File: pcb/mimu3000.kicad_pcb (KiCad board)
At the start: 2 copper layers, 54.9 x 25.9 mm, 14 parts, among them SW1 P_MISO, SW2 P_MOSI, U1 ATTINY13A-SSU, U2 AQY211EH

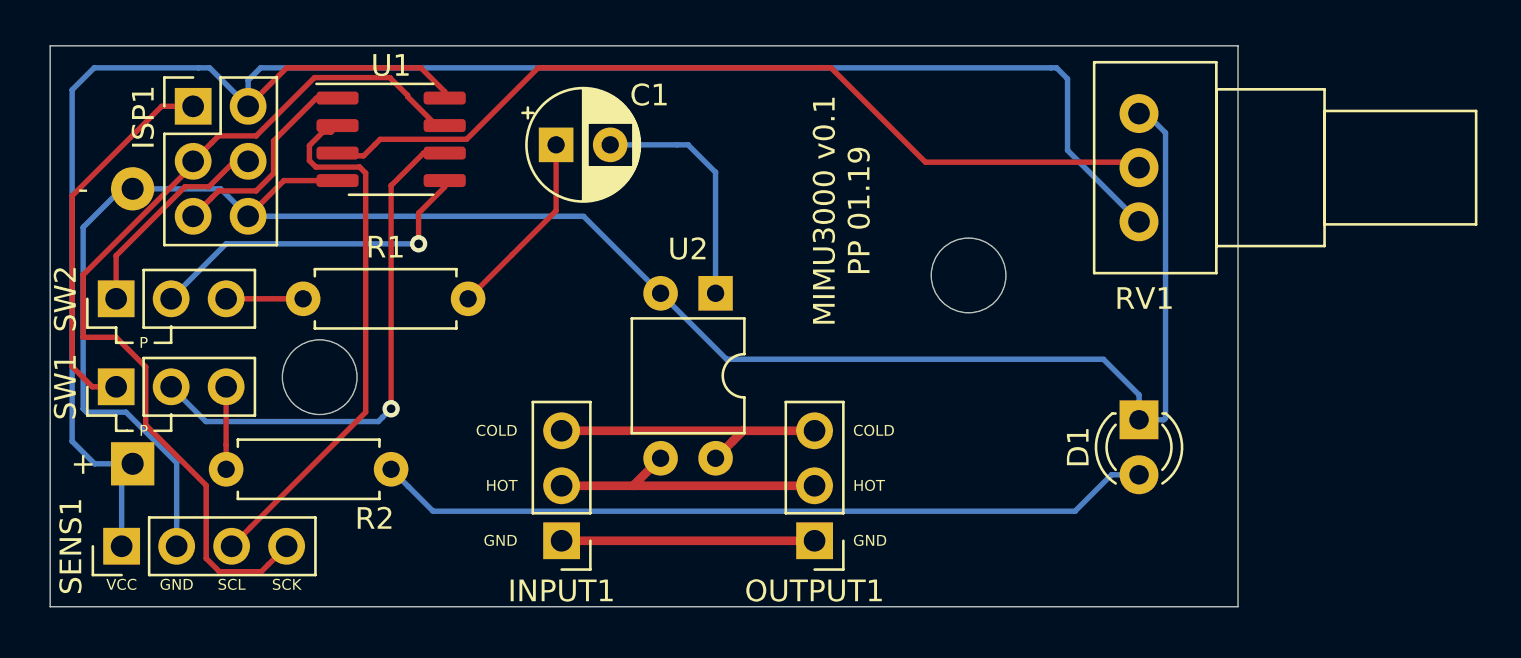
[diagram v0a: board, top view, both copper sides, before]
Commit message: Switched to attiny48
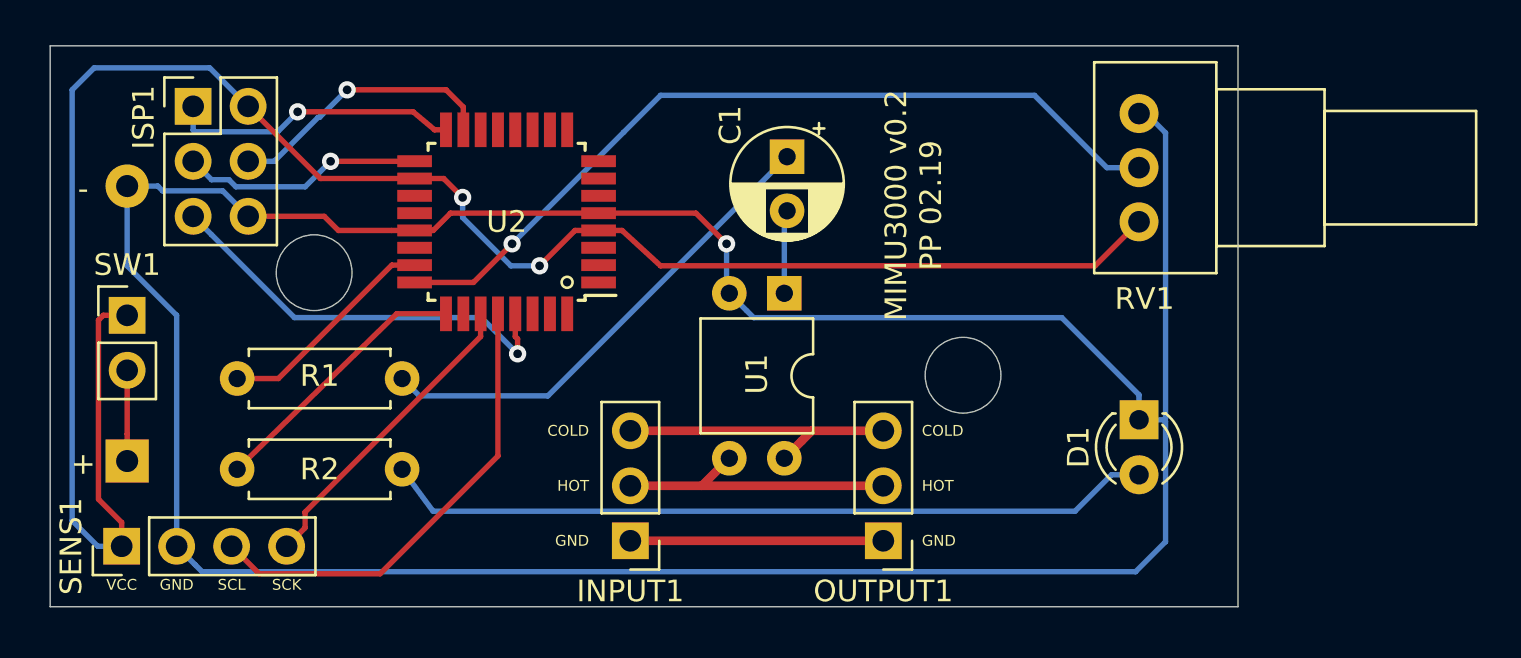
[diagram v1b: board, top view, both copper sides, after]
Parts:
- removed BT1: 3V, Battery:BatteryHolder_Keystone_2468_2xAAA
- removed SW2: P_MOSI, Connector_PinHeader_2.54mm:PinHeader_1x03_P2.54mm_Vertical
- removed the U1 at (179.8, 105.2)
- added BT: 3V, Battery_Holders:Keystone_2468_2xAAA, B.Cu at (167.6, 120.0)
- added U2: ATTINY48U, Housings_QFP:TQFP-32_7x7mm_Pitch0.8mm, F.Cu at (185.2, 109.0)
- R1: value 100R -> 580R
- SW1: value P_MISO -> ONOFF; footprint Connector_PinHeader_2.54mm:PinHeader_1x03_P2.54mm_Vertical -> Pin_Headers:Pin_Header_Straight_1x02_Pitch2.54mm
- moved C1 10.7 mm to (198.1, 106.0), turned to 270 degrees
- moved R1 4.78 mm to (172.7, 116.2)
- moved SW1 3.34 mm to (167.6, 113.3), turned to 0 degrees
- moved INPUT1 3.18 mm to (190.9, 123.7)
- moved OUTPUT1 3.18 mm to (202.6, 123.7)
- moved U1 3.17 mm to (198.0, 112.3)
- moved R2 0.51 mm to (172.7, 120.4)
- renumbered U2 to U1
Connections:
- net Net-(BT1-Pad2) renamed GND
- ISP1 pad 2: Net-(BT1-Pad1) (its old number) -> +3V0
- R1 pad 1: Net-(R1-Pad1) -> MUTE
- R2 pad 1: Net-(R2-Pad1) -> LED
- RV1 pad 1: Net-(BT1-Pad1) (its old number) -> +3V0
- RV1 pad 2: Net-(RV1-Pad2) -> POT
- SENS1 pad 1: Net-(BT1-Pad1) (its old number) -> +3V0
- SENS1 pad 4: Net-(ISP1-Pad3) -> Net-(SENS1-Pad4)
- SW1 pad 1: Net-(ISP1-Pad1) -> +3V0
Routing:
- net +3V0: track 0.00 -> 91.2 mm, vias 0 -> 2
- net Net-(BT1-Pad1) (its old number): track 90.1 -> 0.00 mm
- net GND: track 93.1 -> 140.4 mm, vias 0 -> 1
- net Net-(RV1-Pad2): track 40.7 -> 0.00 mm
- net POT: track 0.00 -> 38.4 mm, vias 0 -> 1
- net Net-(ISP1-Pad3): track 42.3 -> 11.4 mm, vias 0 -> 1
- net Net-(BT1-Pad1): track 24.5 -> 4.19 mm, vias 1 -> 0
- net Net-(SW2-Pad2): track 15.5 -> 0.00 mm, vias 1 -> 0
- net Net-(SENS1-Pad4): track 0.00 -> 14.4 mm
- net Net-(C1-Pad1): track 8.80 -> 22.7 mm
- net LED: track 0.00 -> 12.6 mm
- net MUTE: track 0.00 -> 10.4 mm
- net Net-(ISP1-Pad5): track 9.81 -> 19.5 mm, vias 0 -> 1
- net Net-(C1-Pad2): track 11.0 -> 3.86 mm
- net Net-(ISP1-Pad1): track 17.6 -> 13.5 mm, vias 0 -> 1
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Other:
- board text added: "MIMU3000 v0.2 PP 02.19"
- board text removed: "MIMU3000 v0.1 PP 01.19"
- board text removed: "P"
